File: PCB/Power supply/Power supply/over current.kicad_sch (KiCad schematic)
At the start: 36 parts, among them Q3 IRF9540N, Q4 MMBT3904, Q5 MMBT3906, Q6 IRF540N, U1 LM393, U2 4001, U3 LM393, U4 4001

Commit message: Worked on simulations (ouput stage)
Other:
- note added: "SWITCH"
- note removed: "PASS TRANSISTOR"
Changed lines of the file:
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@@
 		)
 	)
-	(text "PASS TRANSISTOR\n"
+	(text "SWITCH\n"
 		(exclude_from_sim no)
-		(at 233.68 25.146 0)
+		(at 220.726 24.384 0)
 		(effects
 			(font

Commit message: Made Power Supply schematic prettier
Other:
- note added: "SENSE"
- note removed: "COMPARATOR"
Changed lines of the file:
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@@
 		(stroke
 			(width 0.6)
-			(type default)
+			(type dash)
 			(color 132 0 0 1)
 		)
@@
 		(stroke
 			(width 0.6)
-			(type default)
+			(type dash)
 			(color 132 0 0 1)
 		)
@@
 		(stroke
 			(width 0.6)
-			(type default)
+			(type dash)
 			(color 132 0 0 1)
 		)
@@
 		)
 	)
-	(text "COMPARATOR\n"
+	(text "SENSE"
 		(exclude_from_sim no)
-		(at 50.038 25.4 0)
+		(at 43.434 26.416 0)
 		(effects
 			(font
+				(face "AIGDT")
 				(size 3 3)
 				(thickness 0.6)
@@
 	(text "LOGIC"
 		(exclude_from_sim no)
-		(at 130.81 24.638 0)
+		(at 130.81 25.654 0)
 		(effects
 			(font
+				(face "AIGDT")
 				(size 3 3)
 				(thickness 0.6)
@@
 	(text "SWITCH\n"
 		(exclude_from_sim no)
-		(at 220.726 24.384 0)
+		(at 220.726 25.4 0)
 		(effects
 			(font
+				(face "AIGDT")
 				(size 3 3)
 				(thickness 0.6)

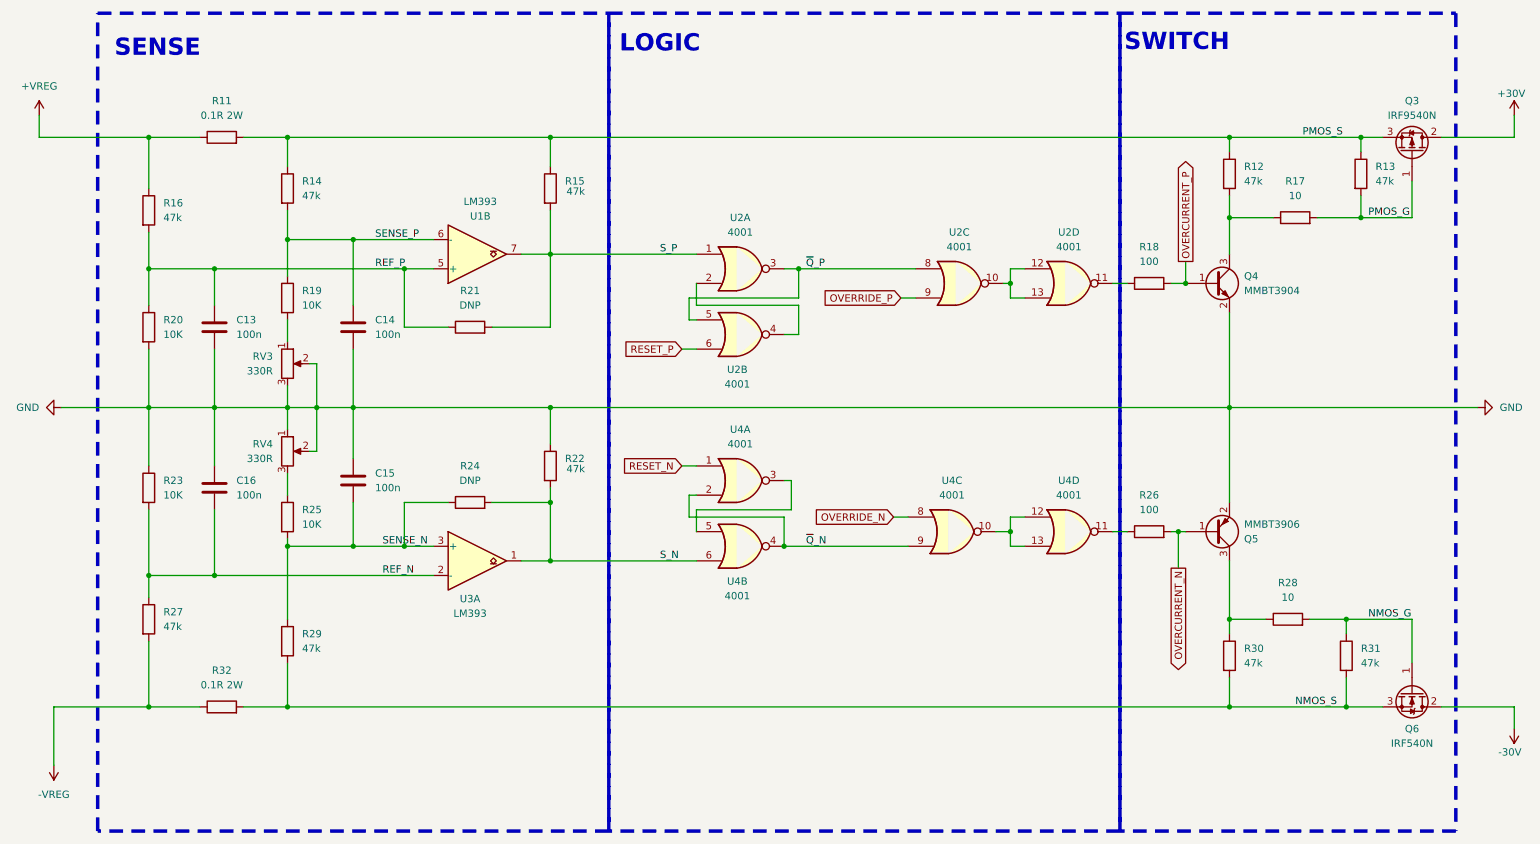
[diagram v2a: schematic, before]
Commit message: Did some simulations, fixed some mistakes in PSU schematic
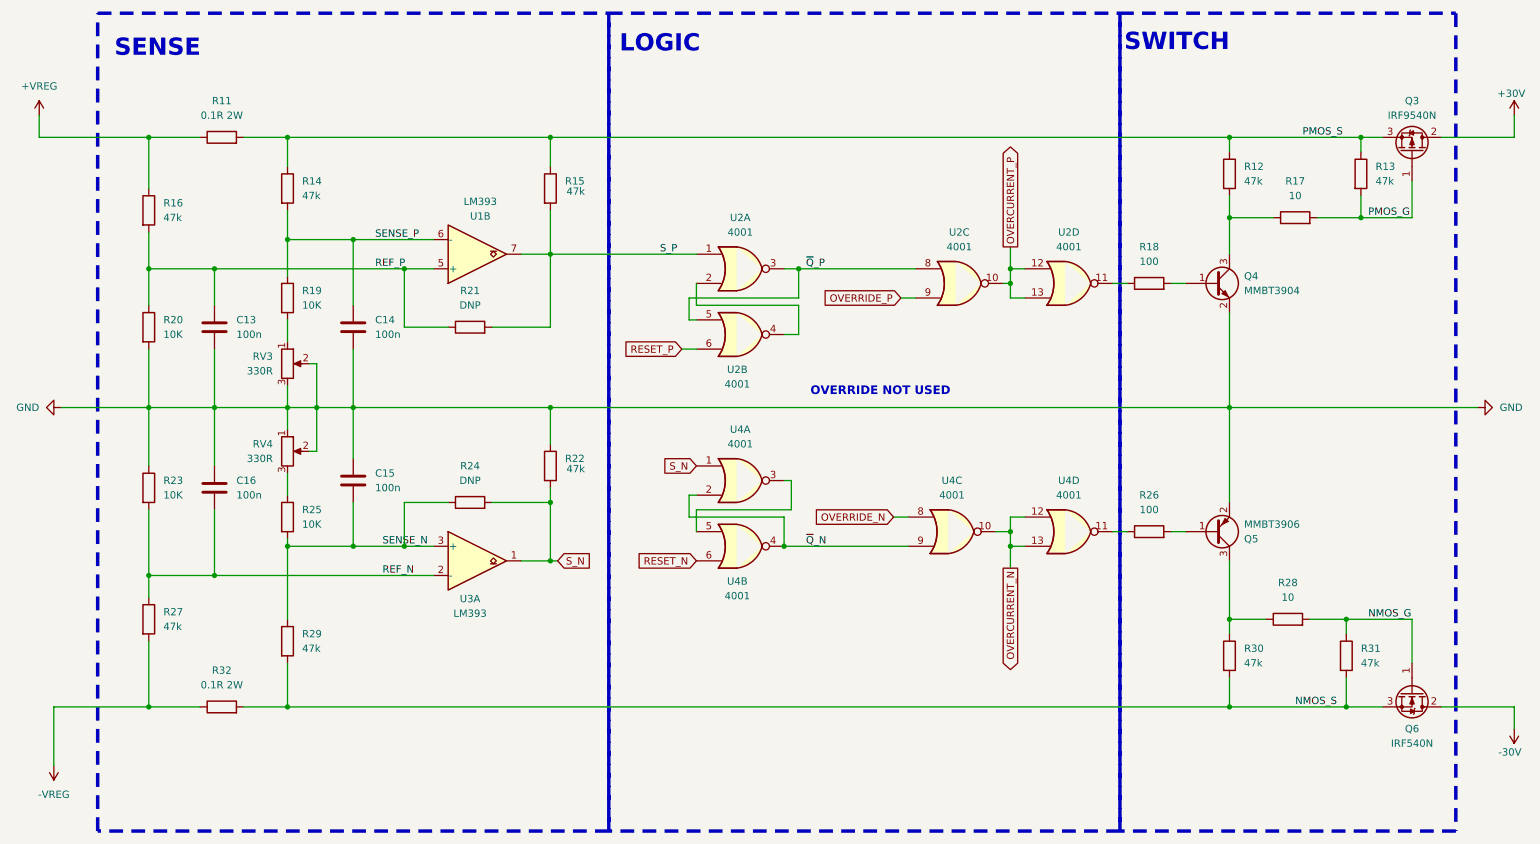
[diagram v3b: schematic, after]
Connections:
- net OVERCURRENT_N: now also U4.10, U4.12, U4.13; no longer Q5.1 (B), R26.2
- net OVERCURRENT_P: now also U2.10, U2.12, U2.13; no longer Q4.1 (B), R18.2
- net RESET_N: now also U4.6; no longer U4.1
- net S_N: now also U4.1; no longer U4.6
- new net: Q5.1 (B), R26.2
- new net: Q4.1 (B), R18.2
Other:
- note added: "OVERRIDE NOT USED"
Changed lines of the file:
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@@
+	)
+	(junction
+		(at 191.77 64.77)
+		(diameter 0)
+		(color 0 0 0 0)
 	)
 	(junction
@@
 	)
 	(junction
-		(at 222.25 67.31)
-		(diameter 0)
-		(color 0 0 0 0)
-	)
-	(junction
 		(at 111.76 105.41)
 		(diameter 0)
@@
 	)
 	(junction
+		(at 66.04 59.69)
+		(diameter 0)
+		(color 0 0 0 0)
+	)
+	(junction
+		(at 250.19 140.97)
+		(diameter 0)
+		(color 0 0 0 0)
+	)
+	(junction
+		(at 71.12 88.9)
+		(diameter 0)
+		(color 0 0 0 0)
+	)
+	(junction
+		(at 229.87 125.73)
+		(diameter 0)
+		(color 0 0 0 0)
+	)
+	(junction
+		(at 77.47 59.69)
+		(diameter 0)
+		(color 0 0 0 0)
+	)
+	(junction
+		(at 252.73 41.91)
+		(diameter 0)
+		(color 0 0 0 0)
+	)
+	(junction
+		(at 191.77 113.03)
+		(diameter 0)
+		(color 0 0 0 0)
+	)
+	(junction
+		(at 154.94 64.77)
+		(diameter 0)
+		(color 0 0 0 0)
+	)
+	(junction
 		(at 111.76 115.57)
 		(diameter 0)
@@
 	)
 	(junction
-		(at 66.04 59.69)
-		(diameter 0)
-		(color 0 0 0 0)
-	)
-	(junction
-		(at 250.19 140.97)
-		(diameter 0)
-		(color 0 0 0 0)
-	)
-	(junction
-		(at 71.12 88.9)
-		(diameter 0)
-		(color 0 0 0 0)
-	)
-	(junction
-		(at 229.87 125.73)
-		(diameter 0)
-		(color 0 0 0 0)
-	)
-	(junction
-		(at 77.47 59.69)
-		(diameter 0)
-		(color 0 0 0 0)
-	)
-	(junction
-		(at 252.73 41.91)
-		(diameter 0)
-		(color 0 0 0 0)
-	)
-	(junction
-		(at 154.94 64.77)
-		(diameter 0)
-		(color 0 0 0 0)
-	)
-	(junction
 		(at 41.91 64.77)
 		(diameter 0)
@@
 	)
 	(junction
-		(at 220.98 110.49)
-		(diameter 0)
-		(color 0 0 0 0)
-	)
-	(junction
 		(at 66.04 140.97)
 		(diameter 0)
@@
 	(wire
 		(pts
-			(xy 220.98 110.49) (xy 222.25 110.49)
+			(xy 219.71 110.49) (xy 222.25 110.49)
 		)
 		(stroke
@@
 	(wire
 		(pts
-			(xy 111.76 115.57) (xy 137.16 115.57)
-		)
-		(stroke
-			(width 0)
-			(type default)
-		)
-	)
-	(wire
-		(pts
 			(xy 194.31 64.77) (xy 191.77 64.77)
 		)
@@
 	(wire
 		(pts
-			(xy 220.98 110.49) (xy 220.98 116.84)
-		)
-		(stroke
-			(width 0)
-			(type default)
-		)
-	)
-	(wire
-		(pts
 			(xy 53.34 64.77) (xy 53.34 71.12)
 		)
@@
 	(wire
 		(pts
+			(xy 191.77 113.03) (xy 191.77 116.84)
+		)
+		(stroke
+			(width 0)
+			(type default)
+		)
+	)
+	(wire
+		(pts
 			(xy 41.91 64.77) (xy 41.91 71.12)
 		)
@@
 	(wire
 		(pts
+			(xy 191.77 60.96) (xy 191.77 64.77)
+		)
+		(stroke
+			(width 0)
+			(type default)
+		)
+	)
+	(wire
+		(pts
 			(xy 53.34 64.77) (xy 86.36 64.77)
 		)
@@
 	(wire
 		(pts
-			(xy 222.25 63.5) (xy 222.25 67.31)
-		)
-		(stroke
-			(width 0)
-			(type default)
-		)
-	)
-	(wire
-		(pts
 			(xy 86.36 105.41) (xy 86.36 113.03)
 		)
@@
 	(wire
 		(pts
-			(xy 134.62 99.06) (xy 137.16 99.06)
-		)
-		(stroke
-			(width 0)
-			(type default)
-		)
-	)
-	(wire
-		(pts
 			(xy 66.04 54.61) (xy 66.04 59.69)
 		)
@@
 	(wire
 		(pts
-			(xy 219.71 110.49) (xy 220.98 110.49)
-		)
-		(stroke
-			(width 0)
-			(type default)
-		)
-	)
-	(wire
-		(pts
 			(xy 209.55 110.49) (xy 212.09 110.49)
 		)
@@
 		(pts
 			(xy 137.16 71.12) (xy 154.94 71.12)
+		)
+		(stroke
+			(width 0)
+			(type default)
+		)
+	)
+	(wire
+		(pts
+			(xy 111.76 115.57) (xy 113.03 115.57)
 		)
 		(stroke
@@
 		)
 	)
+	(text "OVERRIDE NOT USED"
+		(exclude_from_sim no)
+		(at 169.164 86.106 0)
+		(effects
+			(font
+				(face "AIGDT")
+				(size 1.5 1.5)
+				(thickness 0.6)
+				(bold yes)
+				(color 0 0 0 1)
+			)
+		)
+	)
 	(text "SWITCH\n"
 		(exclude_from_sim no)
@@
 		)
 	)
-	(label "S_N"
-		(at 130.81 115.57 0)
-		(fields_autoplaced yes)
-		(effects
-			(font
-				(size 1.27 1.27)
-			)
-			(justify left bottom)
-		)
-	)
 	(label "REF_P"
 		(at 81.28 64.77 0)
@@
 		)
 	)
+	(global_label "S_N"
+		(shape input)
+		(at 137.16 99.06 180)
+		(fields_autoplaced yes)
+		(effects
+			(font
+				(size 1.27 1.27)
+			)
+			(justify right)
+		)
+		(property "Intersheetrefs" "${INTERSHEET_REFS}"
+			(at 130.6672 99.06 0)
+			(effects
+				(font
+					(size 1.27 1.27)
+				)
+				(justify right)
+				(hide yes)
+			)
+		)
+	)
 	(global_label "OVERCURRENT_P"
 		(shape output)
-		(at 222.25 63.5 90)
+		(at 191.77 60.96 90)
 		(fields_autoplaced yes)
 		(effects
@@
 		)
 		(property "Intersheetrefs" "${INTERSHEET_REFS}"
-			(at 222.25 44.8515 90)
+			(at 191.77 42.3115 90)
 			(effects
 				(font
@@
 		)
 	)
+	(global_label "S_N"
+		(shape input)
+		(at 113.03 115.57 0)
+		(fields_autoplaced yes)
+		(effects
+			(font
+				(size 1.27 1.27)
+			)
+			(justify left)
+		)
+		(property "Intersheetrefs" "${INTERSHEET_REFS}"
+			(at 119.5228 115.57 0)
+			(effects
+				(font
+					(size 1.27 1.27)
+				)
+				(justify left)
+				(hide yes)
+			)
+		)
+	)
 	(global_label "OVERCURRENT_N"
 		(shape output)
-		(at 220.98 116.84 270)
+		(at 191.77 116.84 270)
 		(fields_autoplaced yes)
 		(effects
@@
 		)
 		(property "Intersheetrefs" "${INTERSHEET_REFS}"
-			(at 220.98 135.549 90)
+			(at 191.77 135.549 90)
 			(effects
 				(font
@@
 	(global_label "RESET_N"
 		(shape input)
-		(at 134.62 99.06 180)
+		(at 137.16 115.57 180)
 		(fields_autoplaced yes)
 		(effects
@@
 		)
 		(property "Intersheetrefs" "${INTERSHEET_REFS}"
-			(at 123.5916 99.06 0)
+			(at 126.1316 115.57 0)
 			(effects
 				(font
